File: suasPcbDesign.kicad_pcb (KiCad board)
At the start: 4 copper layers, 71.6 x 100 mm, 99 parts, among them J1 SENSE_IB, J2 SPI CS, J4 SPI CTRL, J5 PWM CTRL, J6 JTAG Pinout, J7 USB_C_Receptacle_USB2.0_16P, M3x1 MountingHole_3.2mm_M3, M3x2 MountingHole_3.2mm_M3, M3x3 MountingHole_3.2mm_M3, M3x4 MountingHole_3.2mm_M3, SW1 SW_SPST, SW2 SW_SPST, SW3 SW_SPST, SW4 SW_SPST, SW5 SW_SPST, SW6 SW_SPST, SW7 SW_SPST, U1 74HC138, U2 LMR51625DDC, U3 MCP3562RT-E/ST, U5 TLV77733PDBVR, U6 LMV331, U7 ESP32-S3-WROOM-1, U8 LM66100DCK, U9 USBLC6-2SC6

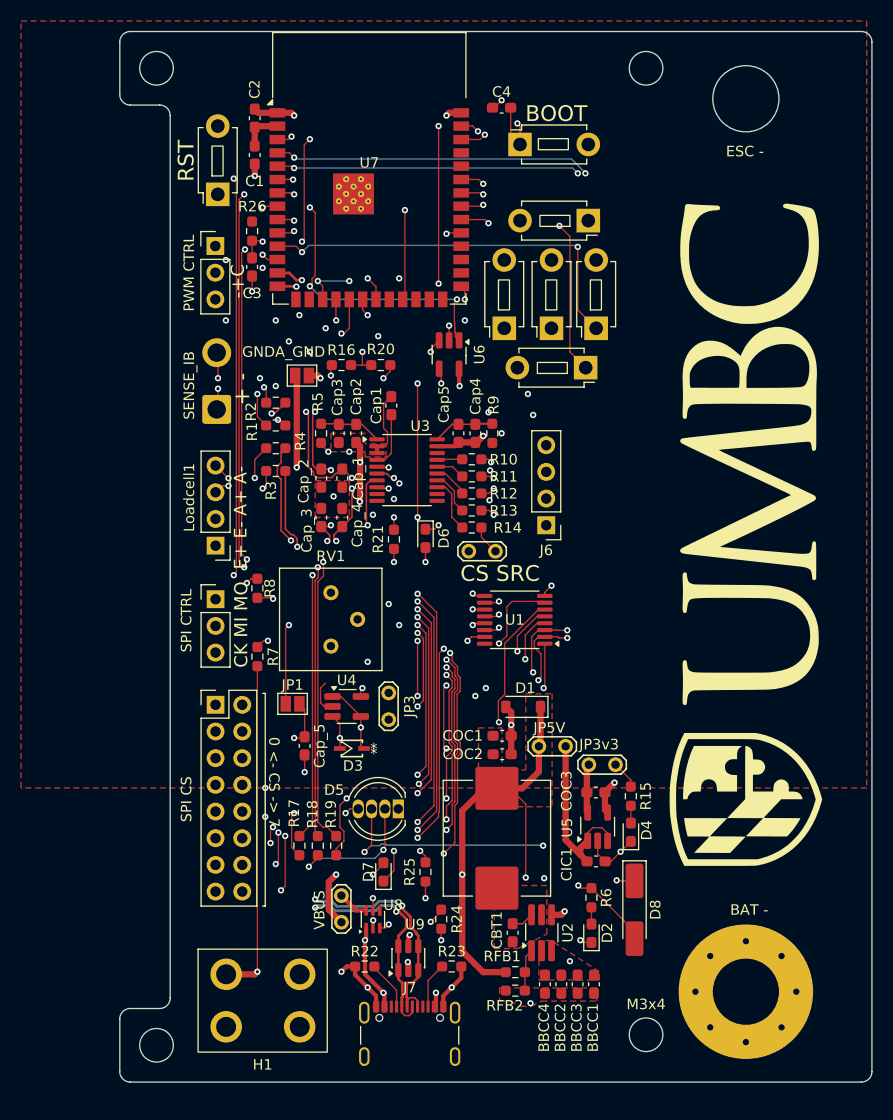
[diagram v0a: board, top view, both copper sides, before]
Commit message: Clean up silscreen notes
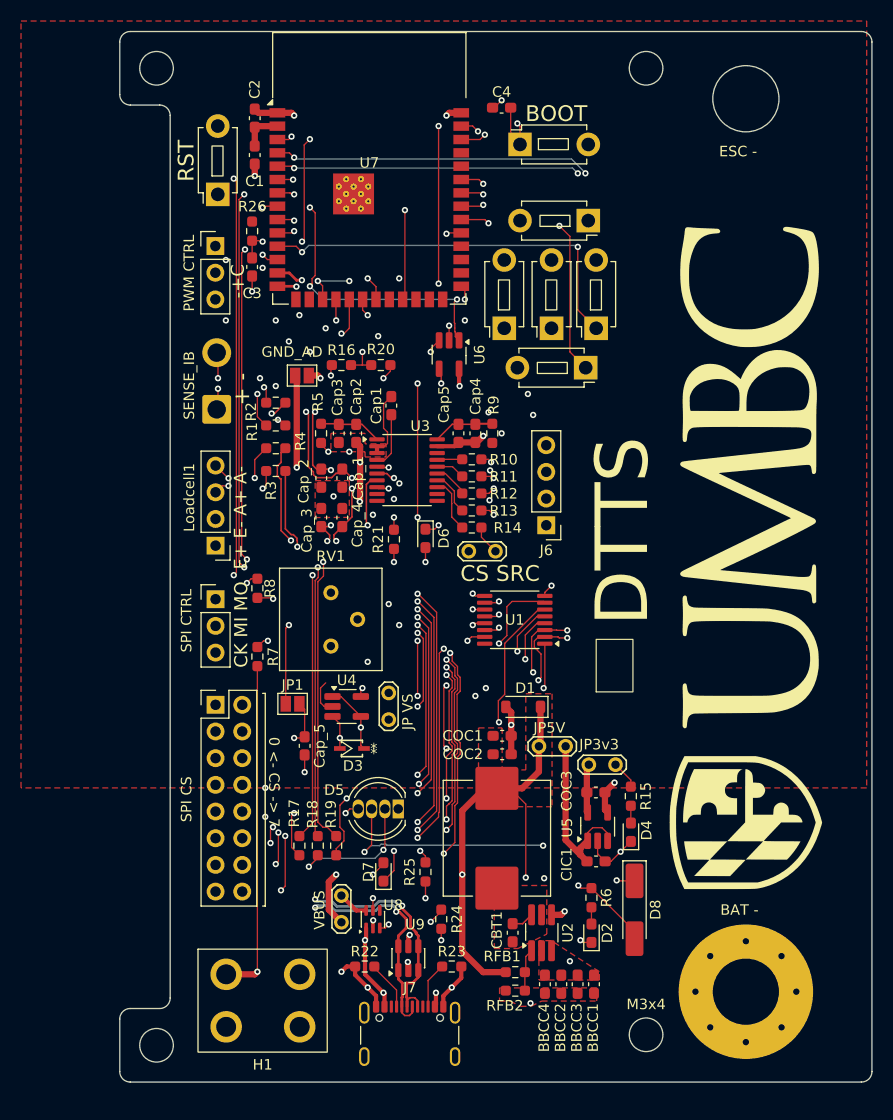
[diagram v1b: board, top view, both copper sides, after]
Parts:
- JP5: value GNDA_GND -> GND_AD
- moved G*** 2.21 mm to (141.5, 140.6)
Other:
- board text added: "DTTS"
- board text added: "JP VS"
- board text added: "󰈐"
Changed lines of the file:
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@@
 			(at 1.25 2 90)
 			(layer "F.SilkS")
+			(hide yes)
 			(effects
 				(font
@@
 	(footprint "Custom:UMBC_Footprint_Official_Large"
 		(layer "F.Cu")
-		(at 141.493547 138.4 90)
+		(at 141.493547 140.605222 90)
 		(property "Reference" "G***"
 			(at 0 0 90)
@@
 			)
 		)
-		(property "Value" "GNDA_GND"
-			(at -1.75 -2.25 180)
+		(property "Value" "GND_AD"
+			(at -0.95 -2.25 180)
 			(layer "F.SilkS")
 			(effects
@@
 		(layer "Edge.Cuts")
 	)
+	(gr_text "JP VS"
+		(at 109.9 157 90)
+		(layer "F.SilkS")
+		(effects
+			(font
+				(size 1 1)
+				(thickness 0.1)
+			)
+			(justify left bottom)
+		)
+	)
 	(gr_text "0 <- CS -> 7"
 		(at 96 157.646429 270)
@@
 	)
 	(gr_text "ESC -"
-		(at 139.6 102.5 0)
+		(at 138.946429 102.5 0)
 		(layer "F.SilkS")
 		(effects
@@
 	)
 	(gr_text "BAT -"
-		(at 140 174.7 0)
+		(at 139.065476 174.7 0)
 		(layer "F.SilkS")
 		(effects
@@
 		)
 	)
+	(gr_text "DTTS"
+		(at 132.7 147.071632 90)
+		(layer "F.SilkS")
+		(effects
+			(font
+				(face "Audiowide")
+				(size 5 5)
+				(thickness 0.2)
+			)
+			(justify left bottom)
+		)
+		(render_cache "DTTS" 90
+			(polygon
+				(pts
+					(xy 130.09572 141.685924) (xy 130.369169 141.738117) (xy 130.6239 141.823463) (xy 130.975565 142.009712)
+					(xy 131.271144 142.25211) (xy 131.511801 142.548911) (xy 131.696432 142.901185) (xy 131.78093 143.155769)
+					(xy 131.832433 143.426963) (xy 131.85 143.717567) (xy 131.85 146.115115) (xy 131.815806 146.293107)
+					(xy 131.722077 146.434768) (xy 131.580416 146.528496) (xy 131.402424 146.56269) (xy 127.39959 146.56269)
+					(xy 127.225566 146.528496) (xy 127.082074 146.434768) (xy 126.986209 146.293107) (xy 126.952015 146.115115)
+					(xy 126.952015 143.717567) (xy 127.840143 143.717567) (xy 127.840143 145.674562) (xy 130.961871 145.674562)
+					(xy 130.961871 143.717567) (xy 130.940312 143.465964) (xy 130.878218 143.244651) (xy 130.776603 143.04463)
+					(xy 130.642524 142.877371) (xy 130.476431 142.741893) (xy 130.277076 142.639845) (xy 130.055304 142.577828)
+					(xy 129.800497 142.556192) (xy 129.001517 142.556192) (xy 128.749442 142.577724) (xy 128.52677 142.639845)
+					(xy 128.325867 142.742002) (xy 128.15949 142.877371) (xy 128.025411 143.04463) (xy 127.923796 143.244651)
+					(xy 127.861702 143.465964) (xy 127.840143 143.717567) (xy 126.952015 143.717567) (xy 126.969615 143.426975)
+					(xy 127.021217 143.155783) (xy 127.105887 142.901185) (xy 127.290343 142.548944) (xy 127.531175 142.25211)
+					(xy 127.722262 142.084283) (xy 127.937681 141.941562) (xy 128.179945 141.823463) (xy 128.435635 141.737991)
+					(xy 128.708529 141.685859) (xy 129.001517 141.668064) (xy 129.800497 141.668064)
+				)
+			)
+			(polygon
+				(pts
+					(xy 127.840143 136.448289) (xy 127.840143 138.405285) (xy 131.85 138.405285) (xy 131.85 139.293413)
+					(xy 127.840143 139.293413) (xy 127.840143 141.253767) (xy 126.952015 141.253767) (xy 126.952015 136.448289)
+				)
+			)
+			(polygon
+				(pts
+					(xy 127.840143 131.368038) (xy 127.840143 133.325033) (xy 131.85 133.325033) (xy 131.85 134.213162)
+					(xy 127.840143 134.213162) (xy 127.840143 136.173516) (xy 126.952015 136.173516) (xy 126.952015 131.368038)
+				)
+			)
+			(polygon
+				(pts
+					(xy 130.408661 126.007518) (xy 130.663578 126.024985) (xy 130.881577 126.074379) (xy 131.082155 126.152998)
+					(xy 131.252215 126.250234) (xy 131.401619 126.369669) (xy 131.525462 126.506384) (xy 131.628659 126.657097)
+					(xy 131.709865 126.810466) (xy 131.815806 127.129814) (xy 131.85 127.435422) (xy 131.85 130.861234)
+					(xy 130.961871 130.861234) (xy 130.961871 127.435422) (xy 130.943683 127.27102) (xy 130.893007 127.141036)
+					(xy 130.811662 127.037612) (xy 130.703718 126.960605) (xy 130.571624 126.912712) (xy 130.408661 126.895646)
+					(xy 130.289126 126.905318) (xy 130.183347 126.933198) (xy 130.08698 126.979315) (xy 130.005661 127.04097)
+					(xy 129.939516 127.117989) (xy 129.889645 127.211635) (xy 129.859047 127.316267) (xy 129.848429 127.435422)
+					(xy 129.848429 129.477903) (xy 129.8302 129.695995) (xy 129.771798 129.942575) (xy 129.672133 130.181457)
+					(xy 129.524197 130.40511) (xy 129.330365 130.597831) (xy 129.076622 130.760484) (xy 128.88712 130.836603)
+					(xy 128.663849 130.884958) (xy 128.400375 130.902144) (xy 128.136892 130.884931) (xy 127.914175 130.836553)
+					(xy 127.725654 130.760484) (xy 127.472957 130.597995) (xy 127.278384 130.40511) (xy 127.129005 130.181338)
+					(xy 127.028951 129.942575) (xy 126.970315 129.695985) (xy 126.952015 129.477903) (xy 126.952015 126.455093)
+					(xy 127.840143 126.455093) (xy 127.840143 129.477903) (xy 127.858618 129.63975) (xy 127.910359 129.768722)
+					(xy 127.994016 129.872356) (xy 128.104002 129.949311) (xy 128.237321 129.997057) (xy 128.400375 130.014016)
+					(xy 128.565598 129.99687) (xy 128.698156 129.948979) (xy 128.805207 129.872356) (xy 128.885636 129.769147)
+					(xy 128.935665 129.640184) (xy 128.953585 129.477903) (xy 128.953585 127.435422) (xy 128.953585 127.428401)
+					(xy 128.992969 127.124623) (xy 129.103794 126.805276) (xy 129.188273 126.650934) (xy 129.293387 126.503025)
+					(xy 129.418371 126.368578) (xy 129.568466 126.248402) (xy 129.738463 126.150068) (xy 129.937273 126.072547)
+					(xy 130.153614 126.02456)
+				)
+			)
+		)
+	)
+	(gr_text "󰈐"
+		(at 126.5 153.971632 0)
+		(layer "F.SilkS")
+		(effects
+			(font
+				(face "FiraCode Nerd Font")
+				(size 5 5)
+				(thickness 0.1)
+			)
+			(justify left bottom)
+		)
+		(render_cache "󰈐" 0
+			(polygon
+				(pts
+					(xy 129.867725 148.076862) (xy 130.114184 148.132515) (xy 130.312325 148.218151) (xy 130.461396 148.332112)
+					(xy 130.564478 148.461023) (xy 130.628009 148.607413) (xy 130.653028 148.765466) (xy 130.637459 148.921304)
+					(xy 130.579771 149.079718) (xy 130.488255 149.22236) (xy 130.369093 149.340109) (xy 130.218902 149.435091)
+					(xy 130.057439 149.541273) (xy 129.923812 149.691235) (xy 129.816441 149.893303) (xy 129.738049 150.160187)
+					(xy 129.937433 150.266768) (xy 130.093422 150.418474) (xy 130.458074 150.253474) (xy 130.810211 150.15299)
+					(xy 131.154047 150.111644) (xy 131.496202 150.131772) (xy 131.776531 150.213621) (xy 132.008286 150.352223)
+					(xy 132.148997 150.493756) (xy 132.250477 150.664247) (xy 132.314134 150.869624) (xy 132.336793 151.118535)
+					(xy 132.316179 151.424051) (xy 132.259402 151.670484) (xy 132.171929 151.868666) (xy 132.057774 152.017967)
+					(xy 131.928755 152.121248) (xy 131.782362 152.18496) (xy 131.624347 152.209815) (xy 131.46912 152.194104)
+					(xy 131.311889 152.136417) (xy 131.171113 152.044202) (xy 131.052675 151.92064) (xy 130.954989 151.761199)
+					(xy 130.844826 151.605661) (xy 130.693499 151.476177) (xy 130.493393 151.37159) (xy 130.233251 151.29439)
+					(xy 130.116382 151.484742) (xy 129.956952 151.649763) (xy 130.122605 152.014409) (xy 130.22357 152.364179)
+					(xy 130.265614 152.703366) (xy 130.246665 153.040593) (xy 130.165568 153.318755) (xy 130.026866 153.550583)
+					(xy 129.885333 153.691294) (xy 129.714842 153.792773) (xy 129.509465 153.856431) (xy 129.260554 153.87909)
+					(xy 128.955062 153.858446) (xy 128.708516 153.801573) (xy 128.510118 153.71392) (xy 128.361011 153.599786)
+					(xy 128.257822 153.470768) (xy 128.194129 153.324353) (xy 128.169273 153.166343) (xy 128.184992 153.011219)
+					(xy 128.242672 152.854186) (xy 128.334877 152.713389) (xy 128.45844 152.594846) (xy 128.61789 152.49698)
+					(xy 128.773117 152.391707) (xy 128.902452 152.244183) (xy 129.007183 152.046367) (xy 129.084699 151.786234)
+					(xy 128.884646 151.668371) (xy 128.729326 151.513292) (xy 128.364663 151.678772) (xy 128.014911 151.779215)
+					(xy 127.675724 151.820428) (xy 127.338381 151.800491) (xy 127.060179 151.719381) (xy 126.828506 151.58168)
+					(xy 126.687843 151.440862) (xy 126.58637 151.270903) (xy 126.522683 151.065825) (xy 126.513604 150.966188)
+					(xy 129.124084 150.966188) (xy 129.144996 151.080368) (xy 129.206516 151.172574) (xy 129.298467 151.234173)
+					(xy 129.411069 151.255006) (xy 129.523881 151.23415) (xy 129.615622 151.172574) (xy 129.677379 151.080343)
+					(xy 129.69836 150.966188) (xy 129.677295 150.852139) (xy 129.615622 150.761635) (xy 129.524044 150.701234)
+					(xy 129.411374 150.68073) (xy 129.298389 150.701237) (xy 129.206516 150.761635) (xy 129.14508 150.852115)
+					(xy 129.124084 150.966188) (xy 126.513604 150.966188) (xy 126.5 150.816895) (xy 126.520146 150.511396)
+					(xy 126.575743 150.263578) (xy 126.661505 150.0631) (xy 126.775779 149.914325) (xy 126.905359 149.811852)
+					(xy 127.052904 149.749248) (xy 127.212029 149.725013) (xy 127.365342 149.740869) (xy 127.517576 149.797486)
+					(xy 127.654372 149.887864) (xy 127.774327 150.011781) (xy 127.878445 150.174536) (xy 127.983906 150.328845)
+					(xy 128.133317 150.457372) (xy 128.335501 150.561228) (xy 128.603541 150.637376) (xy 128.711017 150.438243)
+					(xy 128.865491 150.282003) (xy 128.699993 149.917576) (xy 128.599016 149.5679) (xy 128.55683 149.228706)
+					(xy 128.575963 148.891282) (xy 128.657106 148.6138) (xy 128.795577 148.38332) (xy 128.937134 148.243477)
+					(xy 129.107681 148.142545) (xy 129.313157 148.079198) (xy 129.562194 148.056645)
+				)
+			)
+		)
+	)
 	(segment
 		(start 112.3 122.6)
@@
 		(members "22de6458-355f-4f17-bb94-1a58c7a894bf" "73150530-0241-4595-bf58-92723f993fa7")
 	)
+	(group ""
+		(members "5f32a10e-22e6-4515-847c-507b18ed3661" "d93989ff-4a3a-4735-9f64-48b865b0cde8")
+	)
 	(embedded_fonts no)

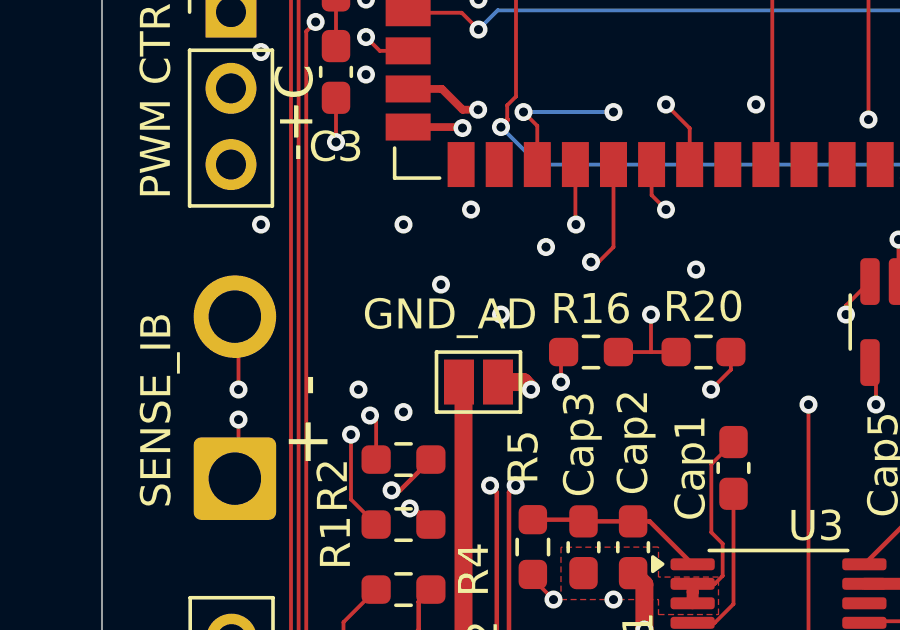
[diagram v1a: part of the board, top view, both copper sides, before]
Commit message: Change resistor value to 100R instead of 50
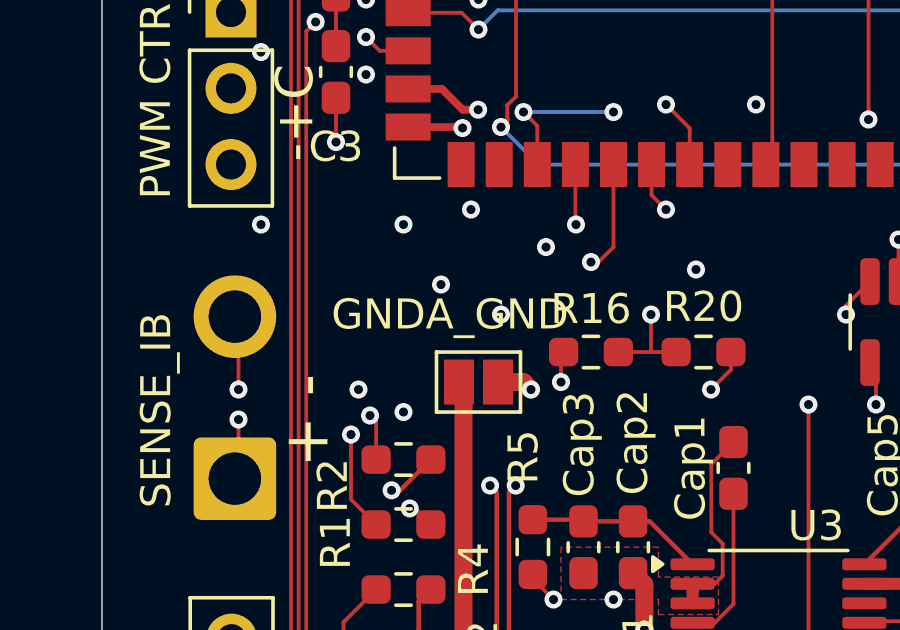
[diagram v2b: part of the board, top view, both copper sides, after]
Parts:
- BBCC1, BBCC2, BBCC3, CIC1, Cap1: value 1uF -> 1u
- BBCC4, CBT1, Cap2, Cap3, Cap4, Cap5, Cap_1, Cap_2, Cap_3, Cap_4: value 0.1uF -> 0.1u
- COC1, COC2: value 47uF -> 47u
- COC3: value 10uF -> 10u
- JP5: value GND_AD -> GNDA_GND
- R1, R2, R3, R4: value 100 -> 100R
- R10, R11, R12, R13, R14, R5, R9: value 10 -> 10R
- R15: value 50R -> 100R
- U4: value ~ -> MCP6486R
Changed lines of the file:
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@@
 			)
 		)
-		(property "Value" "0.1uF"
+		(property "Value" "0.1u"
 			(at 0 1.43 90)
 			(layer "F.Fab")
@@
 			)
 		)
-		(property "Value" "0.1uF"
+		(property "Value" "0.1u"
 			(at -0.776809 3.603314 90)
 			(layer "F.Fab")
@@
 			)
 		)
-		(property "Value" "1uF"
+		(property "Value" "1u"
 			(at 0 1.43 0)
 			(layer "F.Fab")
@@
 			)
 		)
-		(property "Value" "0.1uF"
+		(property "Value" "0.1u"
 			(at 0 1.43 90)
 			(layer "F.Fab")
@@
 			)
 		)
-		(property "Value" "10"
+		(property "Value" "10R"
 			(at 0 1.43 0)
 			(layer "F.Fab")
@@
 			)
 		)
-		(property "Value" "10"
+		(property "Value" "10R"
 			(at -0.273191 -4.493314 90)
 			(layer "F.Fab")
@@
 			)
 		)
-		(property "Value" "100"
+		(property "Value" "100R"
 			(at 0 1.43 0)
 			(layer "F.Fab")
@@
 			)
 		)
-		(property "Value" "47uF"
+		(property "Value" "47u"
 			(at 0 1.43 0)
 			(layer "F.Fab")
@@
 			)
 		)
-		(property "Value" "10"
+		(property "Value" "10R"
 			(at 0 0.963024 0)
 			(layer "F.Fab")
@@
 			)
 		)
-		(property "Value" "100"
+		(property "Value" "100R"
 			(at 0 1.43 0)
 			(layer "F.Fab")
@@
 			)
 		)
-		(property "Value" "0.1uF"
+		(property "Value" "0.1u"
 			(at 0 1.43 90)
 			(layer "F.Fab")
@@
 			)
 		)
-		(property "Value" "0.1uF"
+		(property "Value" "0.1u"
 			(at 0 1.43 90)
 			(layer "F.Fab")
@@
 			)
 		)
-		(property "Value" "47uF"
+		(property "Value" "47u"
 			(at 0 1.43 0)
 			(layer "F.Fab")
@@
 			)
 		)
-		(property "Value" "0.1uF"
+		(property "Value" "0.1u"
 			(at 0 1.43 90)
 			(layer "F.Fab")
@@
 			)
 		)
-		(property "Value" "0.1uF"
+		(property "Value" "0.1u"
 			(at 0 1.43 90)
 			(layer "F.Fab")
@@
 			)
 		)
-		(property "Value" "100"
+		(property "Value" "100R"
 			(at 0 1.43 0)
 			(layer "F.Fab")
@@
 			)
 		)
-		(property "Value" "~"
+		(property "Value" "MCP6486R"
 			(at 0 2.9 0)
 			(layer "F.Fab")
@@
 			)
 		)
-		(property "Value" "1uF"
+		(property "Value" "1u"
 			(at 0 1.43 90)
 			(layer "F.Fab")
@@
 			)
 		)
-		(property "Value" "0.1uF"
+		(property "Value" "0.1u"
 			(at 0 1.094186 90)
 			(layer "F.Fab")
@@
 			)
 		)
-		(property "Value" "10uF"
+		(property "Value" "10u"
 			(at 0 1.43 0)
 			(layer "F.Fab")
@@
 			)
 		)
-		(property "Value" "0.1uF"
+		(property "Value" "0.1u"
 			(at 0 1.43 90)
 			(layer "F.Fab")
@@
 			)
 		)
-		(property "Value" "100"
+		(property "Value" "100R"
 			(at 0 1.43 0)
 			(layer "F.Fab")
@@
 			)
 		)
-		(property "Value" "10"
+		(property "Value" "10R"
 			(at 0 1.43 90)
 			(layer "F.Fab")
@@
 			)
 		)
-		(property "Value" "1uF"
+		(property "Value" "1u"
 			(at 0 1.43 90)
 			(layer "F.Fab")
@@
 			)
 		)
-		(property "Value" "10"
+		(property "Value" "10R"
 			(at 0 1.43 0)
 			(layer "F.Fab")
@@
 			)
 		)
-		(property "Value" "0.1uF"
+		(property "Value" "0.1u"
 			(at 0 1.43 90)
 			(layer "F.Fab")
@@
 			)
 		)
-		(property "Value" "10"
+		(property "Value" "10R"
 			(at -0.0875 0.9325 0)
 			(layer "F.Fab")
@@
 			)
 		)
-		(property "Value" "1uF"
+		(property "Value" "1u"
 			(at 0 -1.09 90)
 			(layer "F.Fab")
@@
 			)
 		)
-		(property "Value" "1uF"
+		(property "Value" "1u"
 			(at 0 1.43 90)
 			(layer "F.Fab")
@@
 			)
 		)
-		(property "Value" "GND_AD"
+		(property "Value" "GNDA_GND"
 			(at -0.95 -2.25 180)
 			(layer "F.SilkS")
@@
 			)
 		)
-		(property "Value" "50R"
+		(property "Value" "100R"
 			(at 0 1.43 90)
 			(layer "F.Fab")
@@
 			)
 		)
-		(property "Value" "10"
+		(property "Value" "10R"
 			(at 0 1.43 0)
 			(layer "F.Fab")
